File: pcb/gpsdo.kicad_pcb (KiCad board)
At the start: 2 copper layers, 151 parts, among them IC1 ICE40LP384-SG32, J1 JTAG, J10 CLK0, J11 CLK7, J12 USB_B_Micro, J13 CLK6, J14 CLK5, J15 CLK4, J2 SSD1306, J3 EXT_CLOCK, J4 GPS_ANT, J5 USB_B_Micro, J6 CLK3, J7 Screw_Terminal_01x03, J8 CLK2, J9 CLK1, M1 E73-2G4M08S1C-52840, Q1 S9018, SW1 EC11, SW2 MCML4-112B, U1 MCP9808_MSOP, U2 MCP9808_MSOP, U3 TPS652510, U4 LT1763xS8, U5 74LVC1G17, U6 Si5351C-B-GM, U7 74LVC1G17, U8 uBlox NEO-7M, U9 AD5761R, Y1 32768, Y2 8663-XS

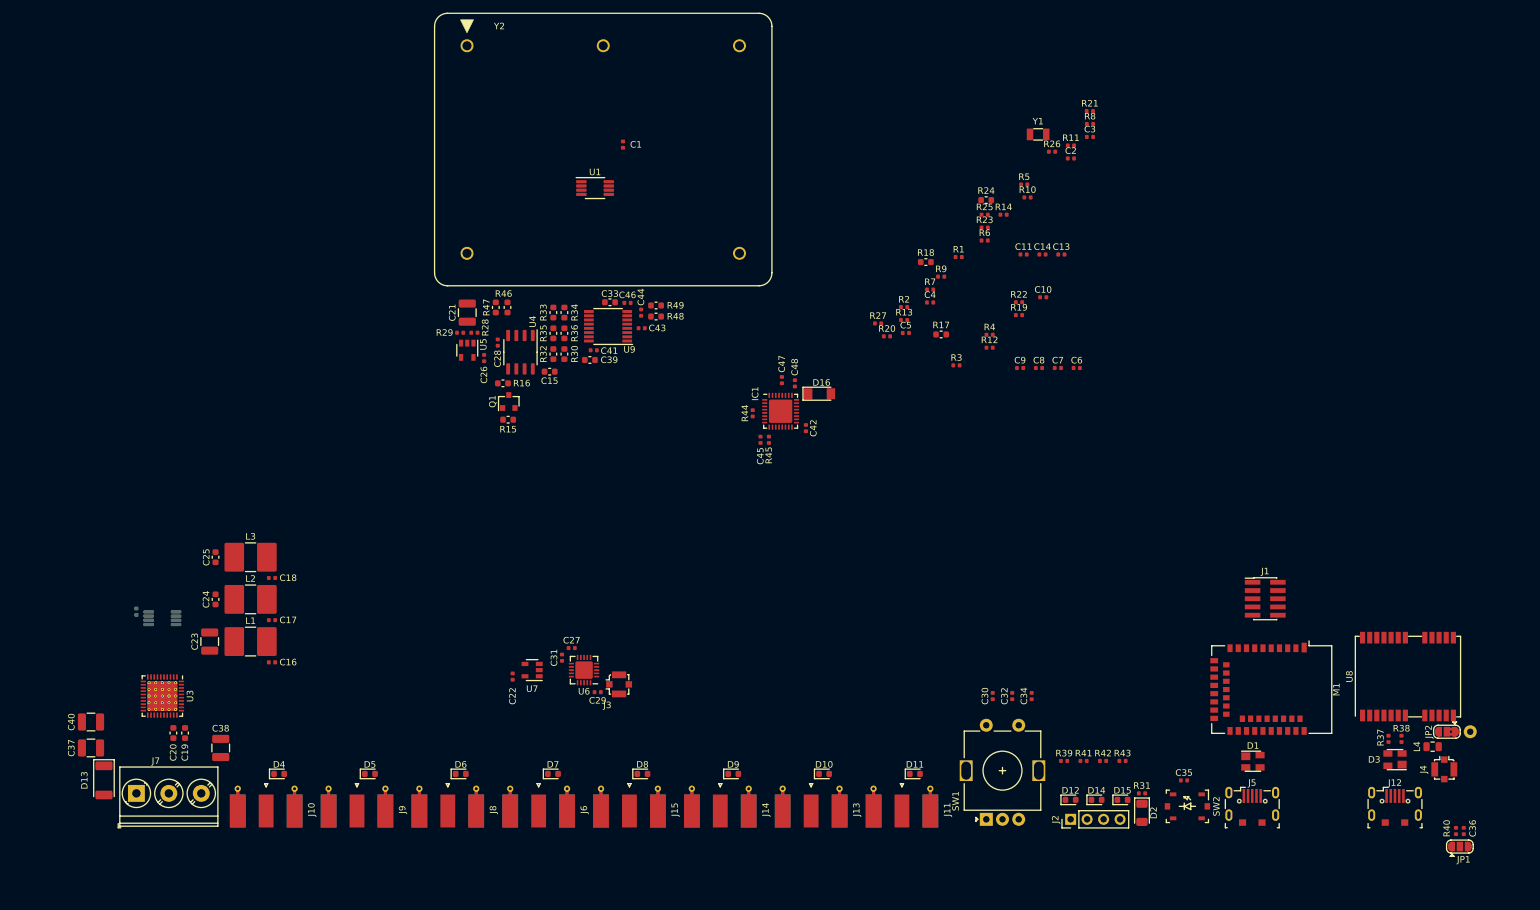
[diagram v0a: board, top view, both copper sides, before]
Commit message: tps652510 routing, inductor footprint
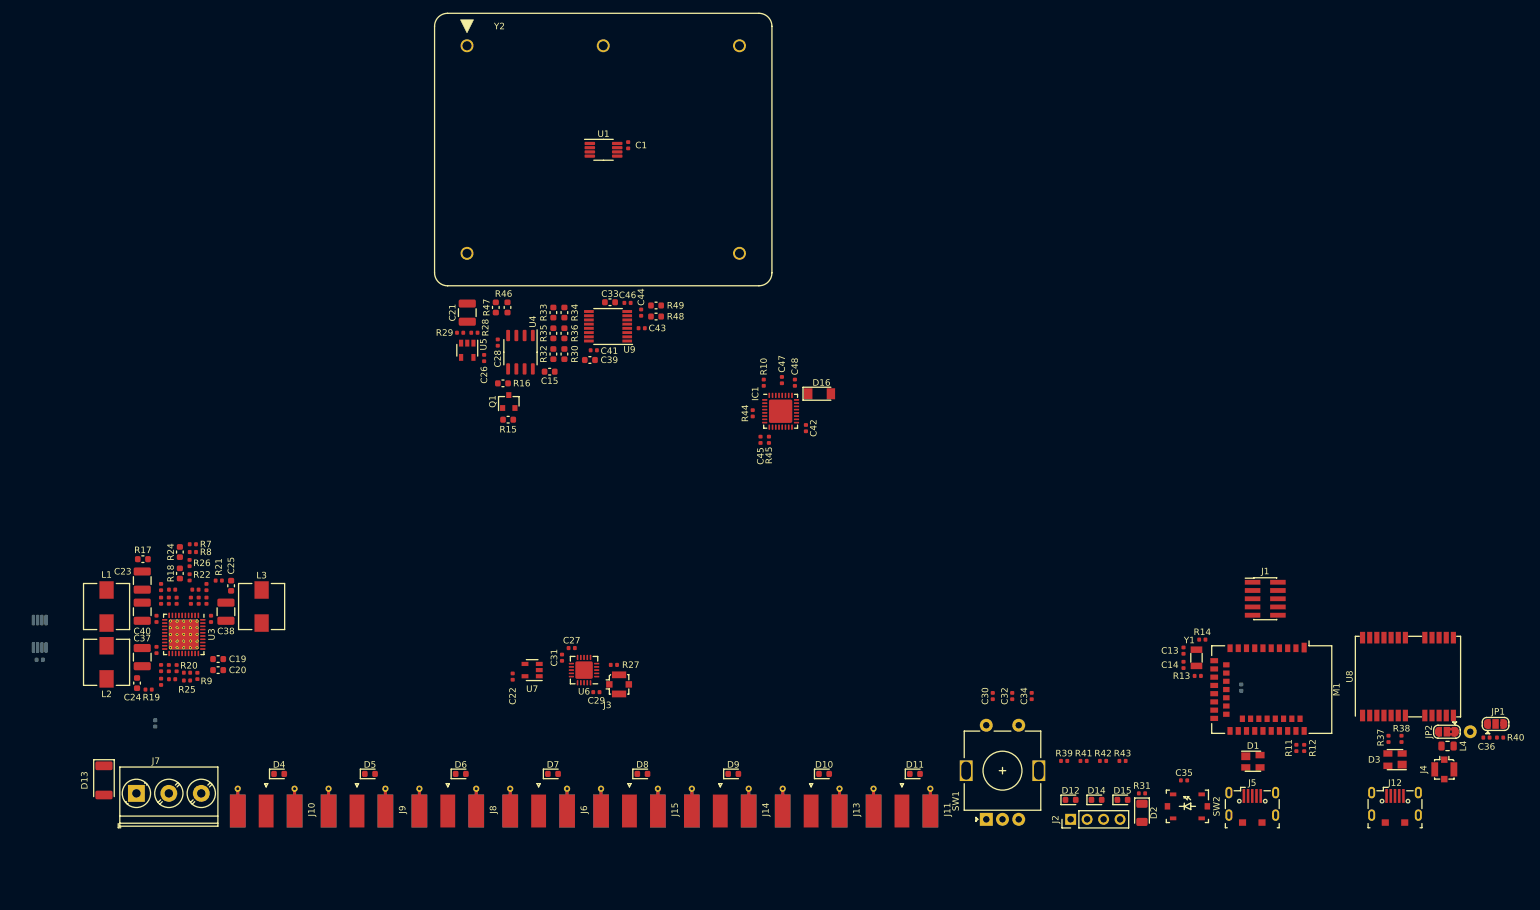
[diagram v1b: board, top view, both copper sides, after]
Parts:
- C11, R23: moved to B.Cu
- L1, L2, L3: footprint Inductor_SMD:L_2816_7142Metric -> Inductor_SMD:L_Wuerth_HCI-7050
- moved C3 164.3 mm to (54.5, 126.4), turned to 180 degrees
- moved C2 153.7 mm to (54.5, 112.6), turned to 180 degrees
- moved R8 153.2 mm to (57.7, 106.8)
- moved R21 152.5 mm to (61.7, 111.2)
- moved C11 152.1 mm to (51.9, 133.2), turned to 270 degrees
- moved R26 147.3 mm to (57.2, 108.5), turned to 270 degrees
- moved R19 146.0 mm to (50.9, 128.0), turned to 180 degrees
- moved C6 145.6 mm to (52.8, 114.3), turned to 270 degrees
- moved C7 144.6 mm to (54.0, 124.7), turned to 90 degrees
- moved R5 143.6 mm to (57.4, 114.3), turned to 90 degrees
- moved C8 143.0 mm to (52.8, 124.7), turned to 90 degrees
- moved R25 142.4 mm to (56.8, 126.6)
- moved R4 138.5 mm to (52.8, 126.8), turned to 270 degrees
- moved C10 137.2 mm to (59.8, 114.3), turned to 270 degrees
- moved R24 135.6 mm to (55.7, 106.8), turned to 270 degrees
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
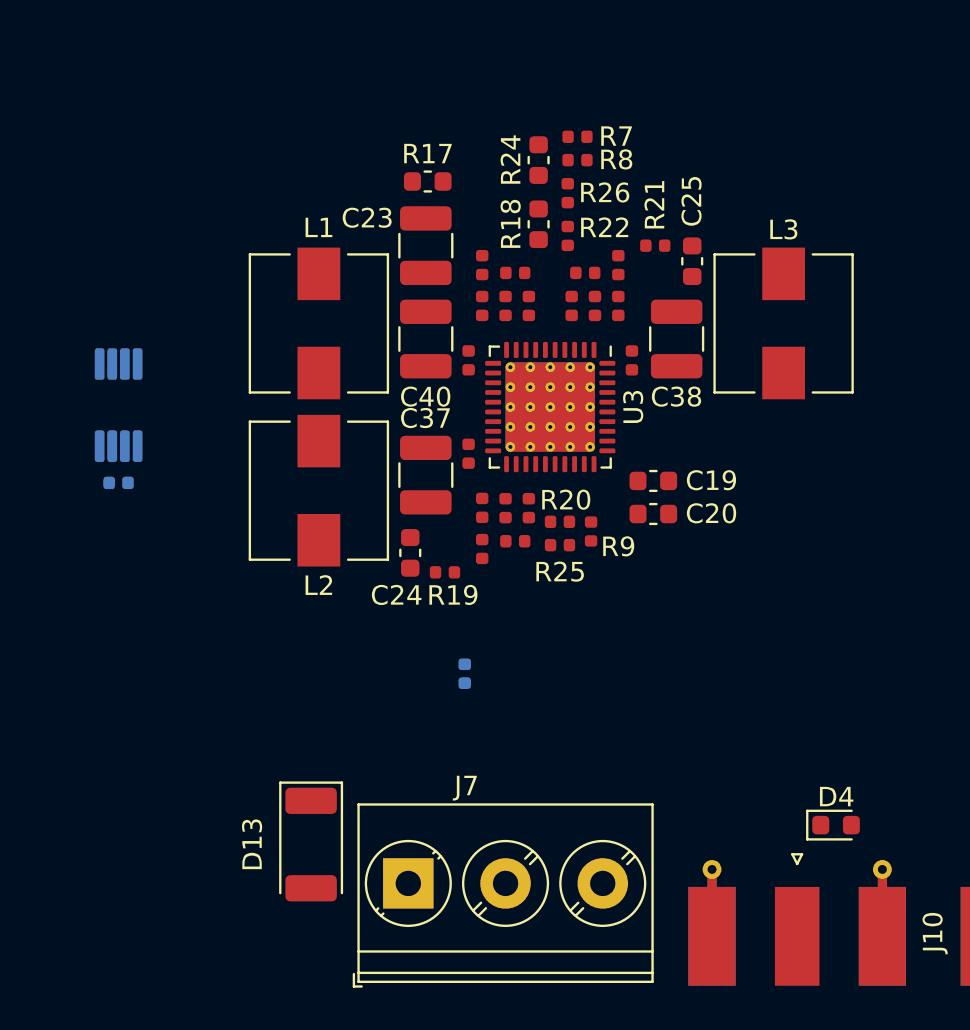
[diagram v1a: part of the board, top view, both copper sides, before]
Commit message: tps652510 routing
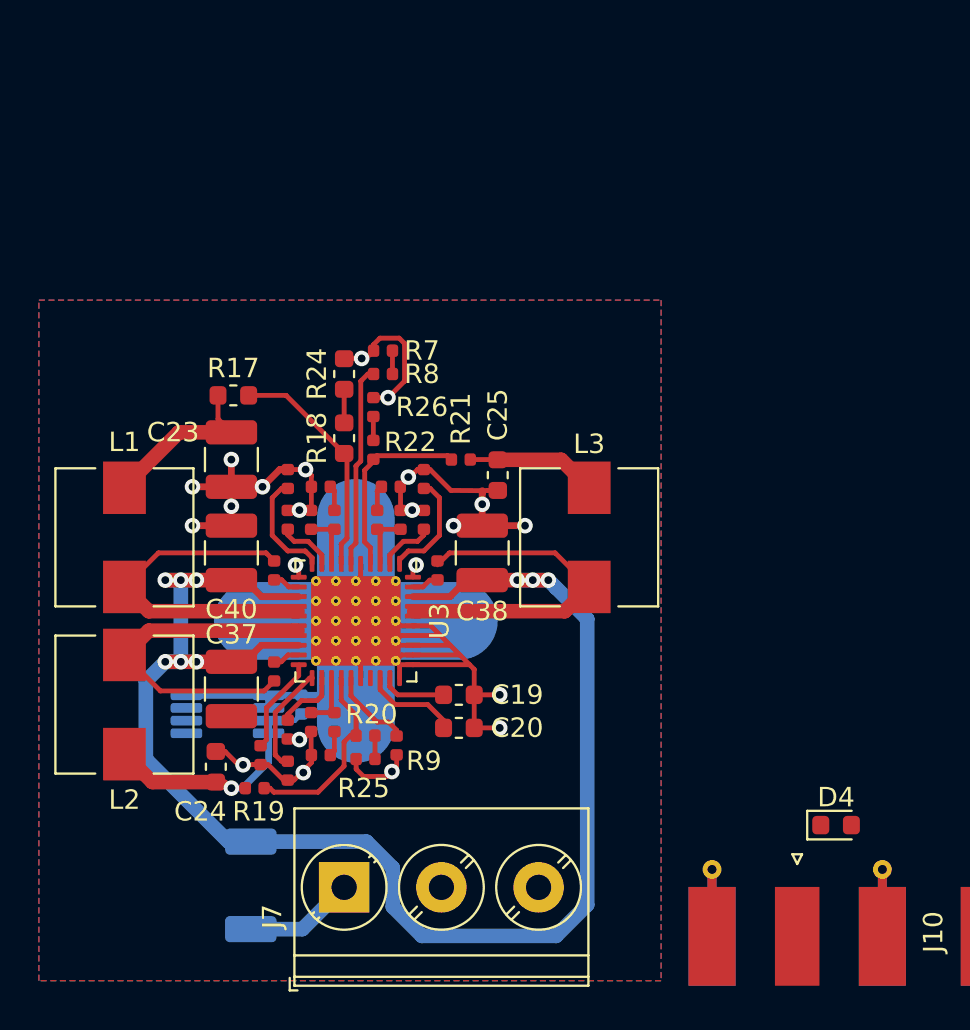
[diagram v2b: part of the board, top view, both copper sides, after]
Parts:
- C11: moved to F.Cu
- D13: moved to B.Cu
- moved U2 16.9 mm to (39.7, 135.3), turned to 0 degrees
- moved C8 15.2 mm to (42.8, 136.1)
- moved R4 15.2 mm to (42.8, 138.2)
- moved C17 15.0 mm to (42.1, 133.1)
- moved C19 14.9 mm to (51.6, 134.3)
- moved L2 14.9 mm to (34.4, 134.8)
- moved C10 14.9 mm to (49.8, 125.3)
- moved C2 14.9 mm to (44.5, 123.6)
- moved C20 14.9 mm to (51.6, 136.0)
- moved C23 14.9 mm to (39.9, 122.2)
- moved C24 14.9 mm to (39.1, 138.0)
- moved C25 14.9 mm to (53.6, 123.0)
- moved C3 14.9 mm to (44.5, 137.4)
- moved C37 14.9 mm to (39.9, 134.0)
- moved C38 14.9 mm to (52.8, 127.0)
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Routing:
- net GND: track 0.00 -> 103.4 mm, vias 0 -> 20
- net +15V: track 0.00 -> 93.0 mm, vias 0 -> 9
- net Net-(C18-Pad1): track 0.00 -> 18.3 mm
- net Net-(C16-Pad1): track 0.00 -> 18.2 mm
- net Net-(C17-Pad1): track 0.00 -> 18.1 mm
- net +3V3: track 0.00 -> 13.4 mm, vias 0 -> 1
- net Net-(R17-Pad1): track 0.00 -> 12.0 mm
- net Net-(R8-Pad1): track 0.00 -> 10.4 mm
- net Net-(R19-Pad1): track 0.00 -> 10.0 mm
- net Net-(R21-Pad1): track 0.00 -> 9.86 mm
- net +12V: track 0.00 -> 8.89 mm
- net +1V2: track 0.00 -> 6.72 mm
- net Net-(R2-Pad1): track 0.00 -> 5.77 mm
- net Net-(R6-Pad1): track 0.00 -> 5.71 mm
- net Net-(D13-Pad2): track 0.00 -> 5.69 mm
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- added copper zone on B.Cu, net GND
- added copper zone on F.Cu, net GND

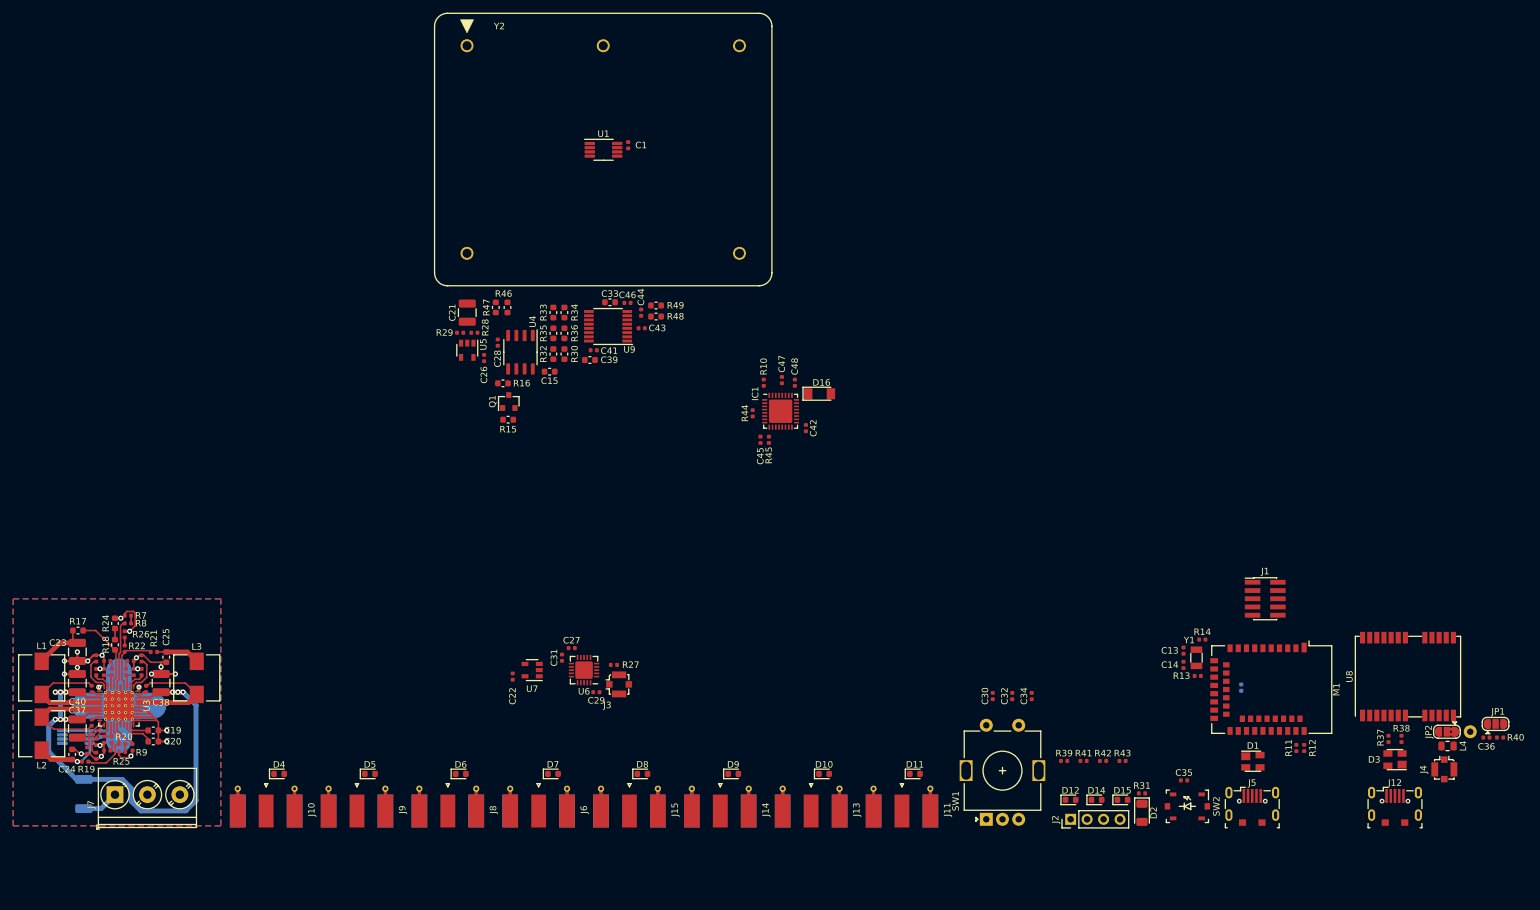
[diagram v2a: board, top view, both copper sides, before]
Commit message: basic component placement and board layout
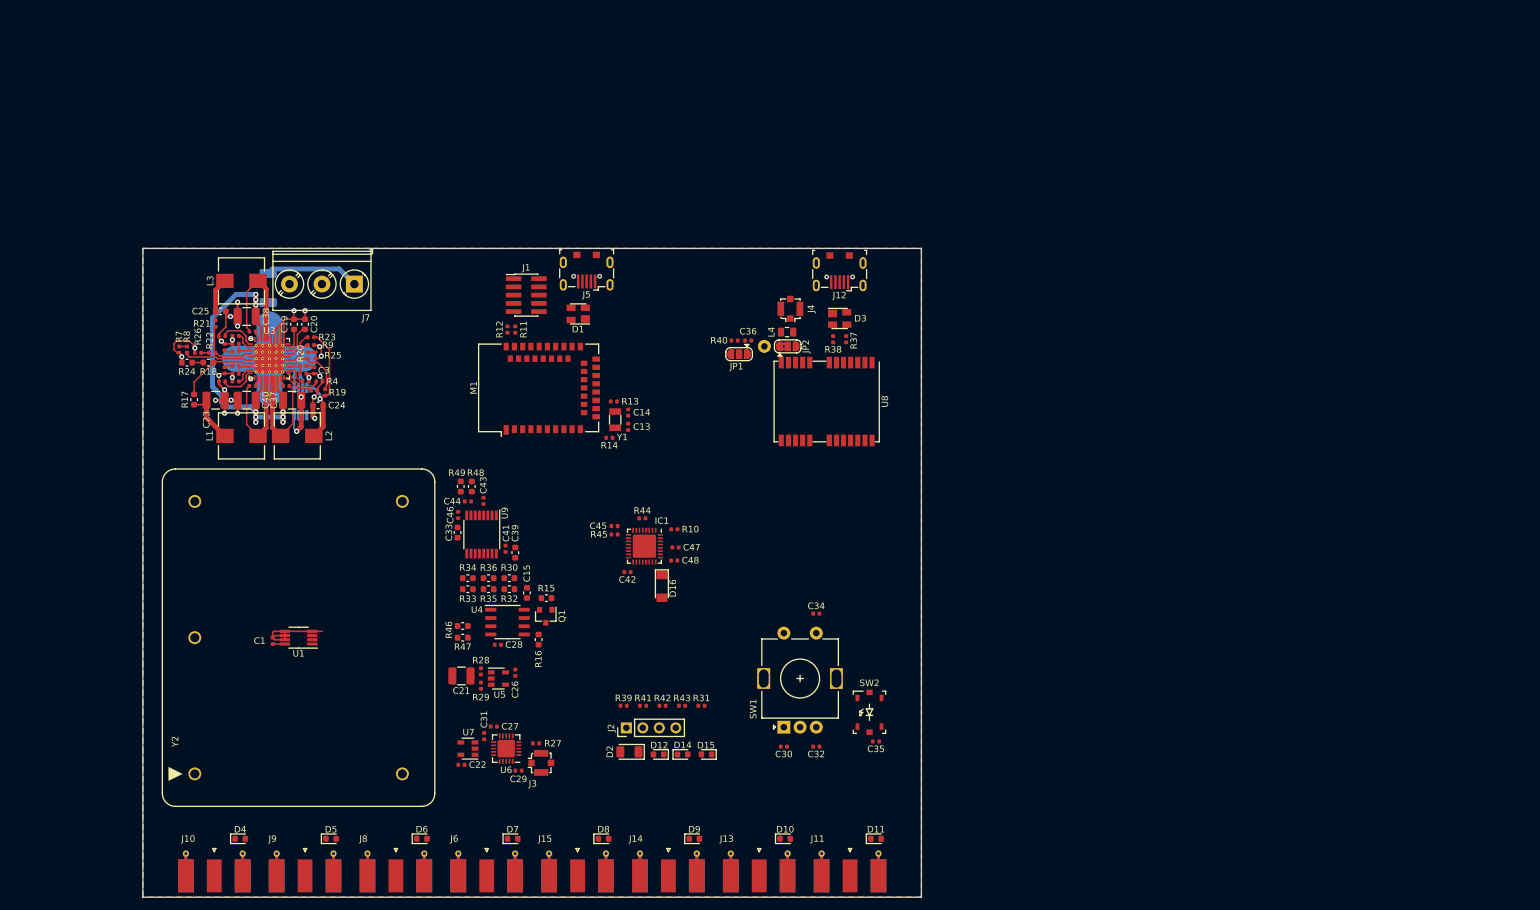
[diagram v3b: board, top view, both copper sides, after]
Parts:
- R23: moved to F.Cu
- moved R23 153.2 mm to (75.9, 73.7), turned to 180 degrees
- moved R12 138.7 mm to (106.2, 72.5), turned to 270 degrees
- moved R11 136.6 mm to (107.4, 72.5), turned to 270 degrees
- moved R40 132.9 mm to (141.2, 74.2), turned to 180 degrees
- moved J5 131.7 mm to (118.4, 63.5), turned to 180 degrees
- moved JP1 129.8 mm to (141.9, 76.3), turned to 180 degrees
- moved C36 129.2 mm to (143.3, 74.2), turned to 0 degrees
- moved D1 124.8 mm to (117.1, 70.1), turned to 180 degrees
- moved AE1 124.0 mm to (145.8, 75.1), turned to 180 degrees
- moved J4 123.3 mm to (149.8, 69.3), turned to 0 degrees
- moved J1 123.1 mm to (109.1, 67.2)
- moved M1 122.2 mm to (111.0, 81.5), turned to 270 degrees
- moved L4 120.1 mm to (149.3, 72.9), turned to 180 degrees
- moved J12 118.8 mm to (157.4, 63.6), turned to 180 degrees
- moved JP2 117.7 mm to (149.4, 75.1), turned to 0 degrees
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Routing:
- net +15V: track 93.0 -> 69.4 mm
- net GND: track 103.4 -> 124.5 mm, vias 20 -> 24
- net +3V3: track 13.4 -> 25.8 mm
- net Net-(D13-Pad2): track 5.69 -> 14.5 mm
- net /PGOOD: track 0.00 -> 4.39 mm
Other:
- board outline added: 120 x 100 mm
